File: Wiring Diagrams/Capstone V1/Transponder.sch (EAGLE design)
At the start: 16 parts, among them J1 ARD_H1, J2 ARD_H2, U1 LLC, U2 MIC5211-LXYM6-TR

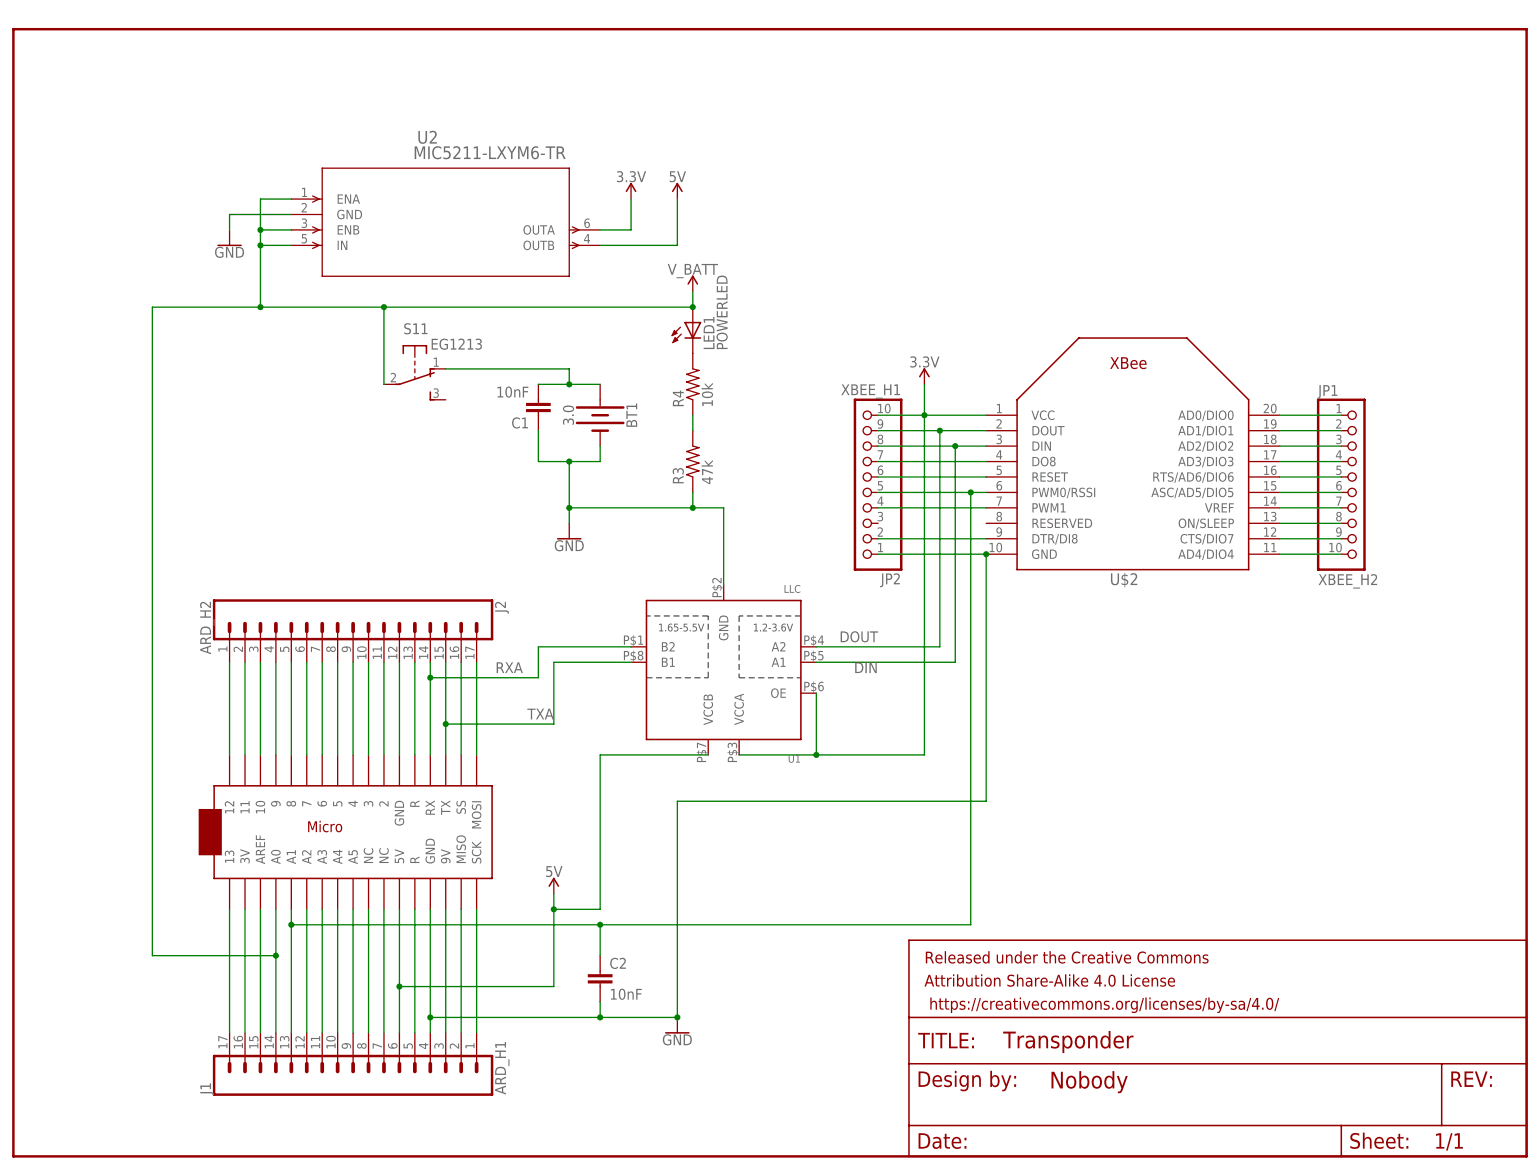
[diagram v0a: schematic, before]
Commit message: Updated wire diagrams for transponder to removed smd
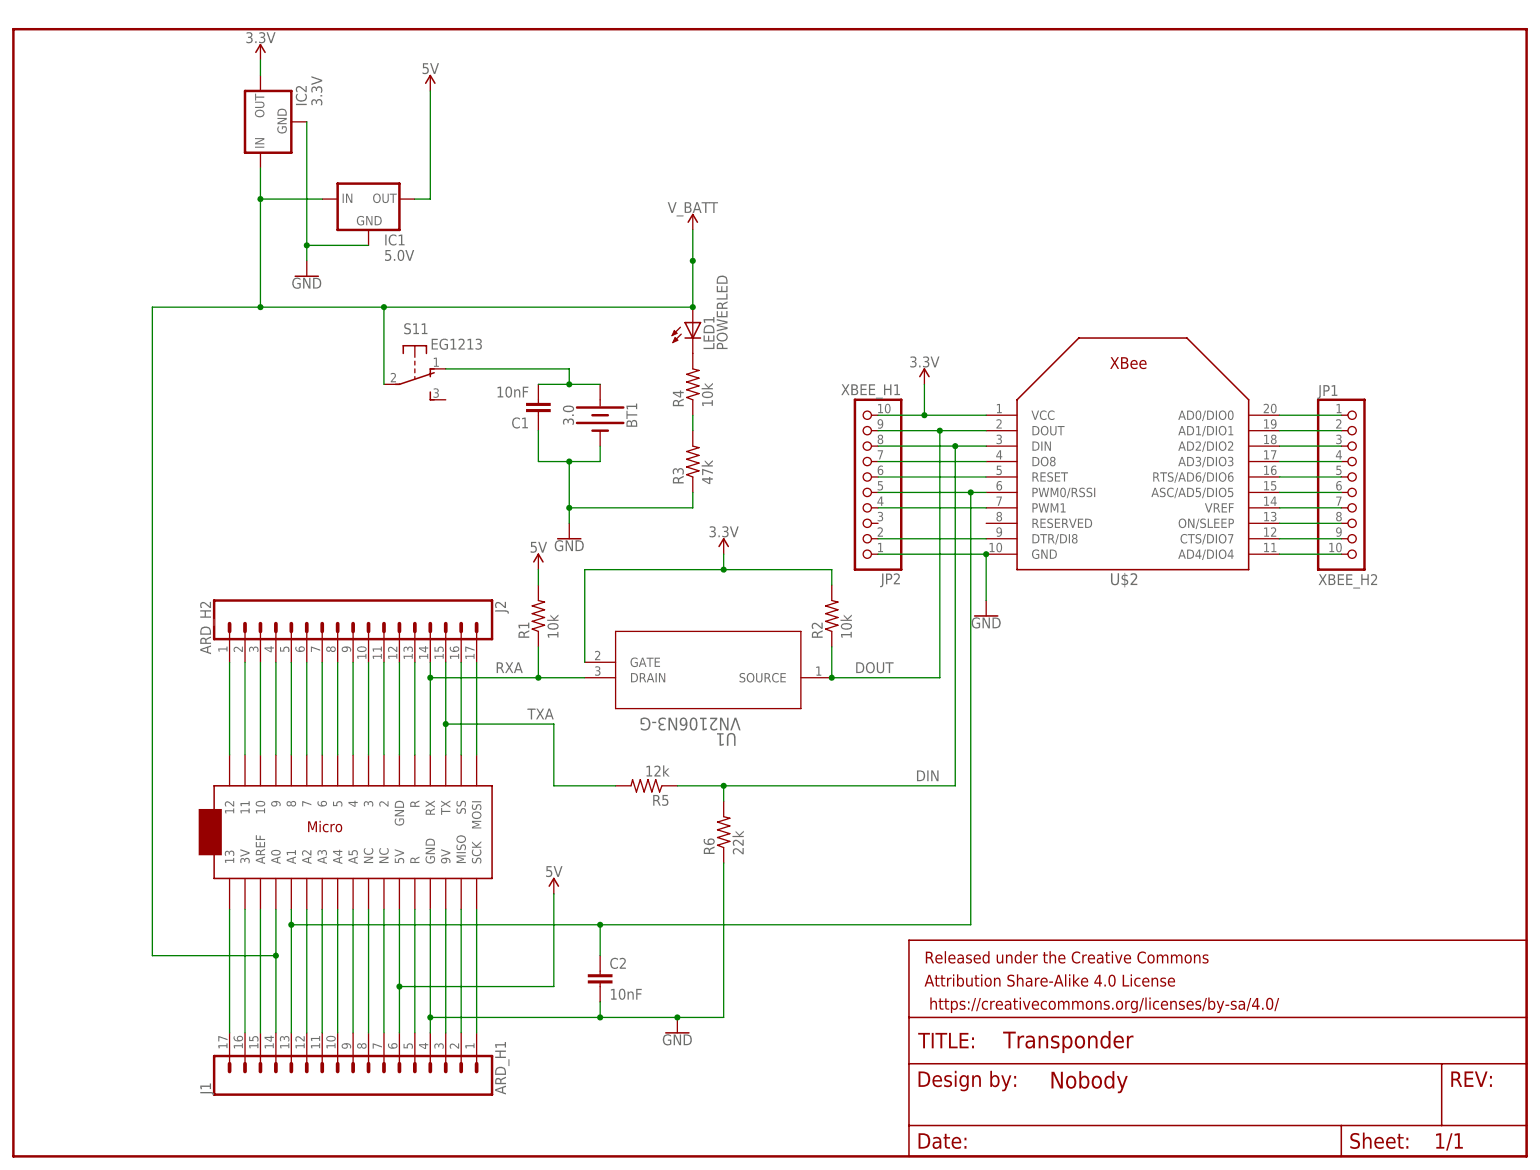
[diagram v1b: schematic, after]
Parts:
- removed U2: MIC5211-LXYM6-TR, MIC5211-LXYM6-TR:MIC5211-LXYM6-TR
- added IC1: 5.0V, adafruit:MCP1700INLINE
- added IC2: 3.3V, adafruit:MCP1700INLINE
- added R1, R2: 10k, resistor:R-US_0207/12
- added R5: 12k, resistor:R-US_0207/12
- added R6: 22k, resistor:R-US_0207/12
- U1: value LLC -> VN2106N3-G; device adafruit:TXS0102 -> VN2106N3-G:VN2106N3-G
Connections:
- net 3.3V: now also IC2.OUT, R2.2, U1.GATE; no longer U1.OE, U1.VCCA, U2.OUTA
- net 5V: now also IC1.OUT, R1.2; no longer U1.VCCB, U2.OUTB
- net DIN: now also R5.1, R6.2; no longer U1.A1
- net DOUT: now also R2.1, U1.SOURCE; no longer U1.A2
- net GND: now also IC1.GND, IC2.GND, R6.1; no longer U1.GND, U2.GND
- net RXA: now also R1.1, U1.DRAIN; no longer U1.B2
- net TXA: now also R5.2; no longer U1.B1
- net V_BATT: now also IC1.IN, IC2.IN; no longer U2.ENA, U2.ENB, U2.IN

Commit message: Added datasheets, made transponder pcb files
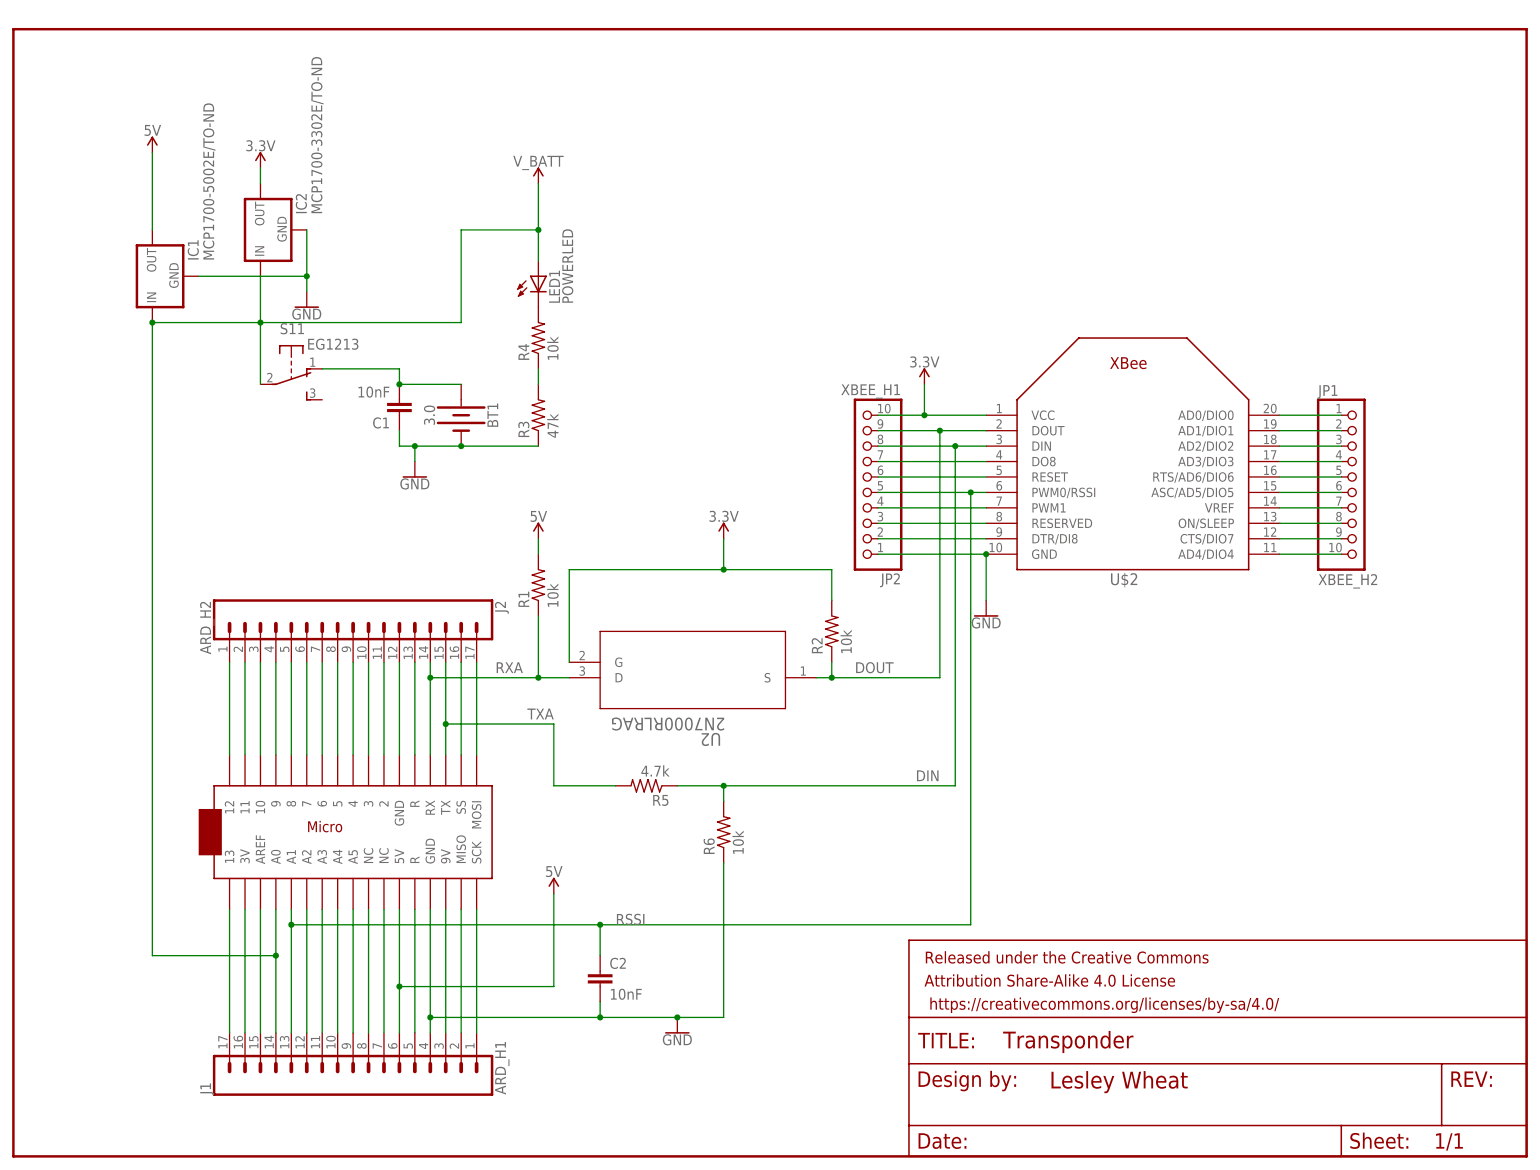
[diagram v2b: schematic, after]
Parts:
- removed U1: VN2106N3-G, VN2106N3-G:VN2106N3-G
- added U2: 2N7000RLRAG, 2N7000RLRAG:2N7000RLRAG
- FRAME1: DESIGNER (none) -> Lesley Wheat
- IC1: value 5.0V -> MCP1700-5002E/TO-ND
- IC2: value 3.3V -> MCP1700-3302E/TO-ND
- J1, J2: device SparkFun-Connectors:CONN_17 -> SparkFun-Connectors:CONN_17NOSILK
- R5: value 12k -> 4.7k
- R6: value 22k -> 10k
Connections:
- net N$48 renamed RSSI
- new net N$2: JP2.3, U$2.RESERVED
- net 3.3V: now also U2.G; no longer U1.GATE
- net DOUT: now also U2.S; no longer U1.SOURCE
- net RXA: now also U2.D; no longer U1.DRAIN
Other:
- moved on the sheet: BT1, C1, IC1, IC2, LED1, R1, R2, R3, R4, S11
